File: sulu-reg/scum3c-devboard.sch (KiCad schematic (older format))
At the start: 36 parts, among them J1 Conn_02x11_Odd_Even, J2 Conn_02x10_Odd_Even, J3 Conn_02x05_Odd_Even, J4 Conn_01x01_Male, U2 S-85S1AB18-I6T1U, U3 S-85S1AB11-I6T1U, U9AB1 ICM-20948

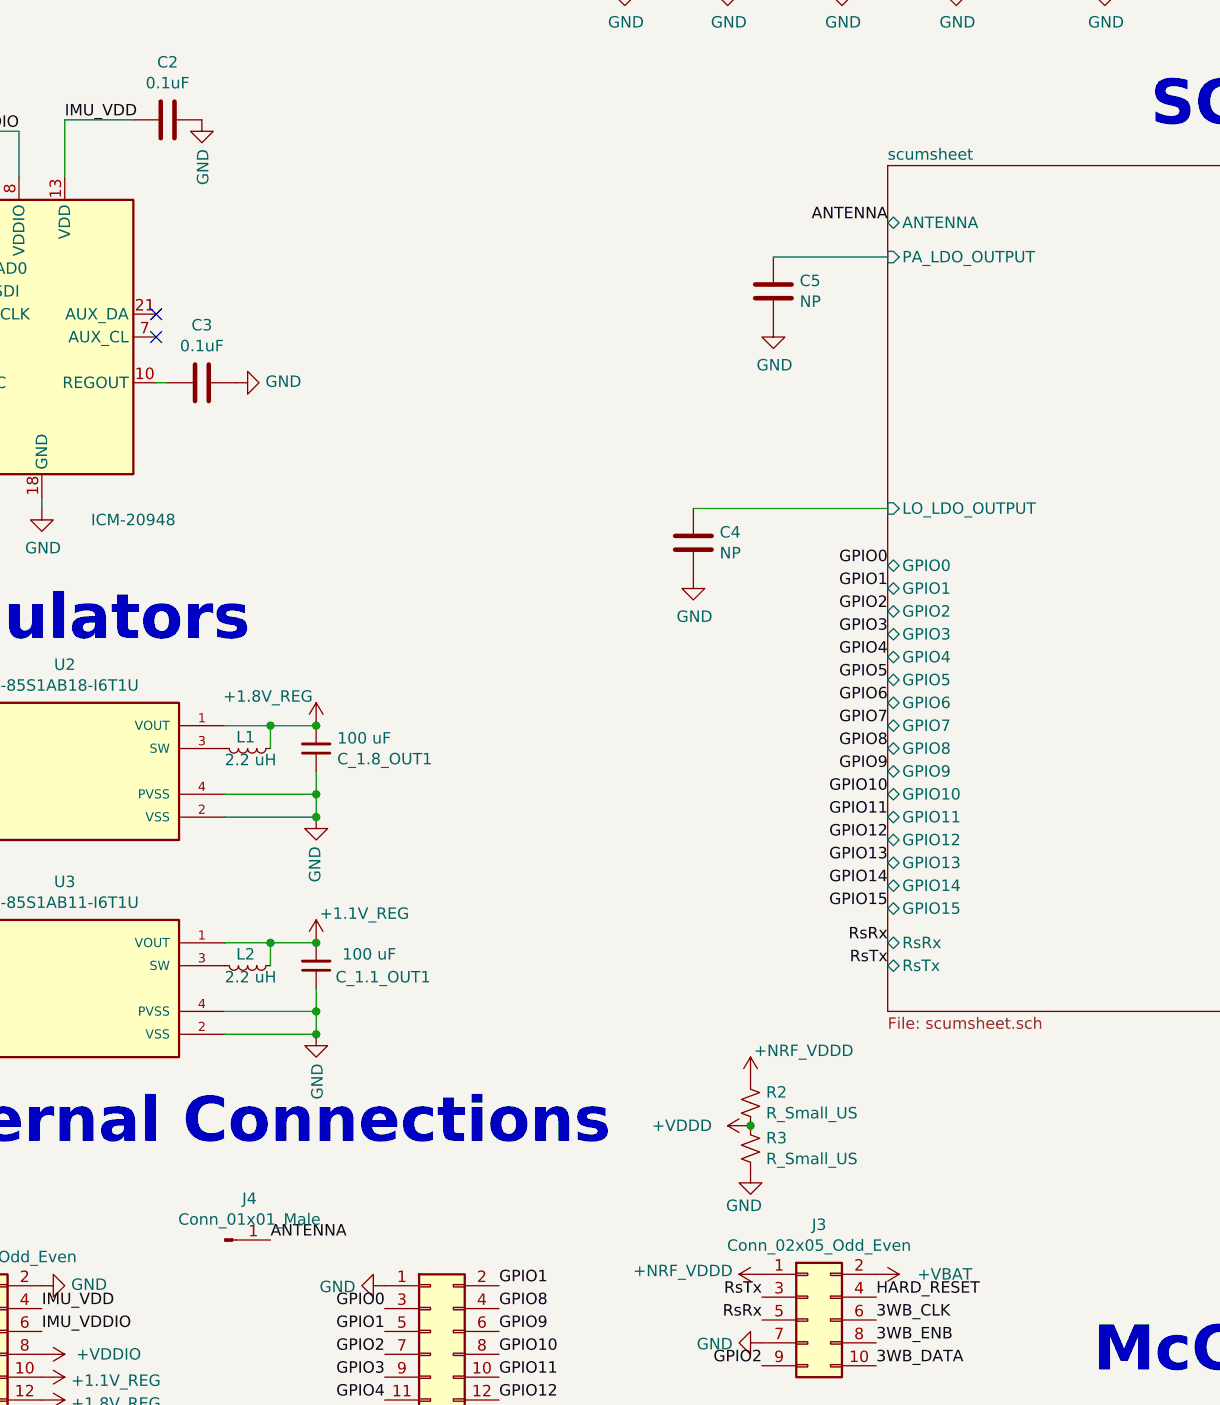
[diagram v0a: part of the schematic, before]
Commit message: added coax connector, not connected in layout
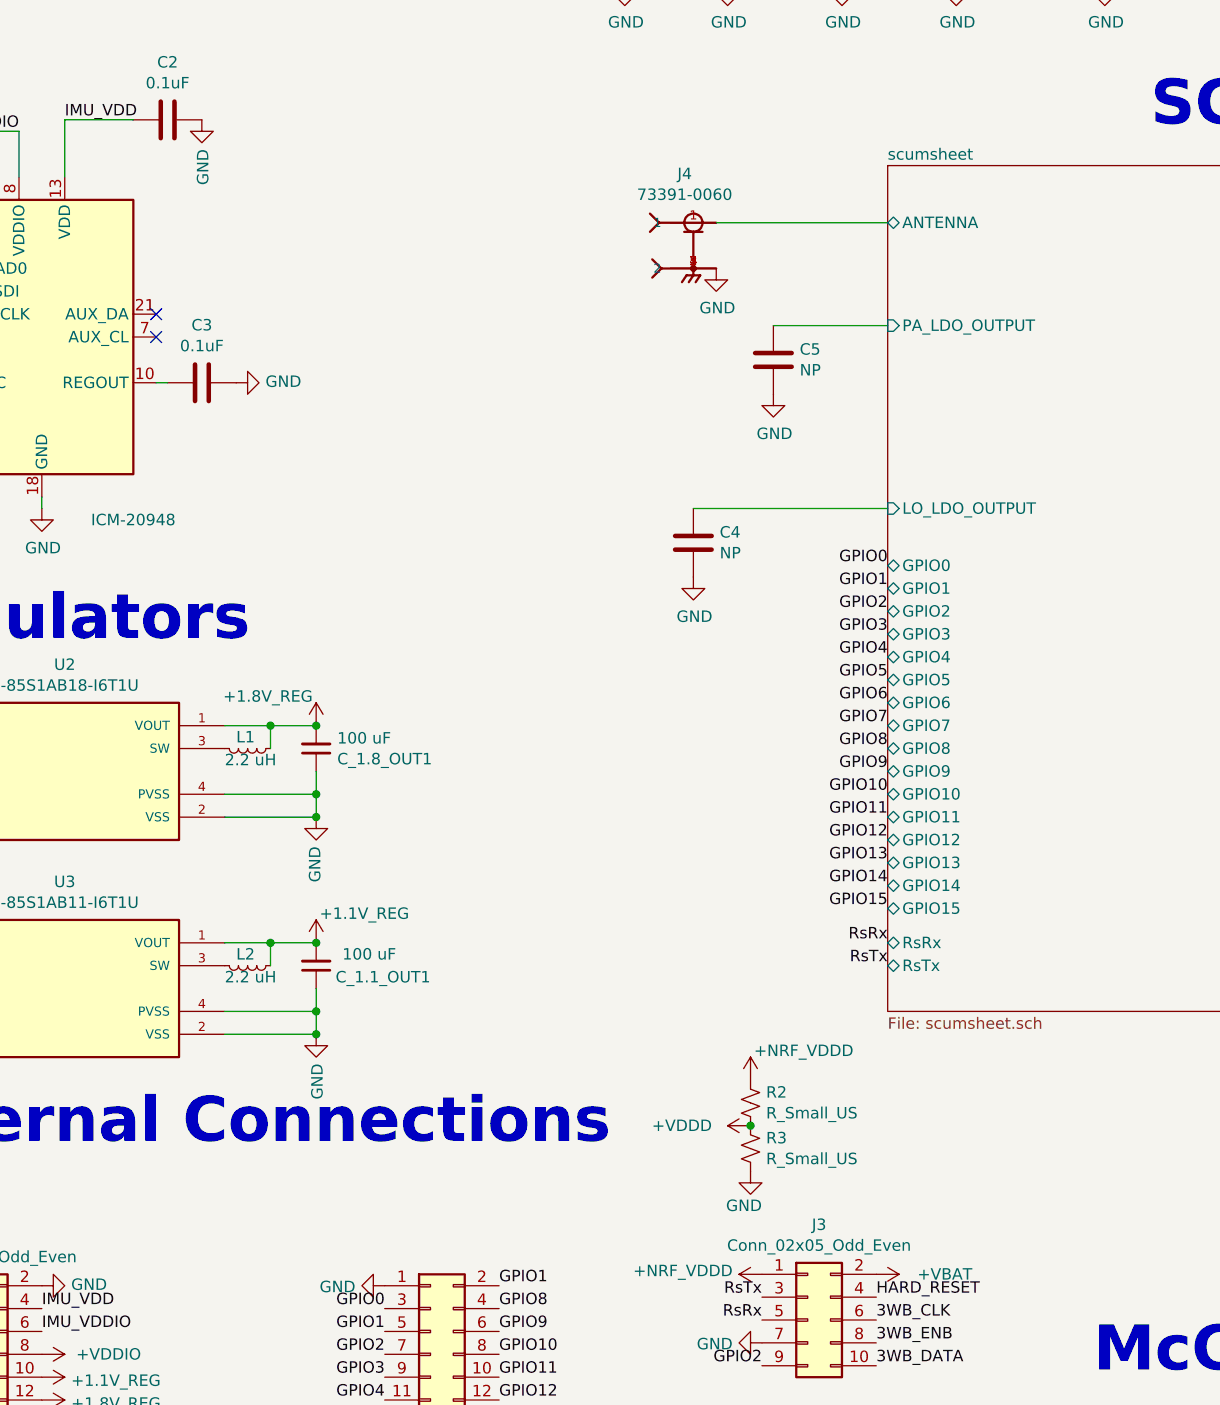
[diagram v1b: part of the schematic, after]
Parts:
- removed J4: Conn_01x01_Male, Connector_PinHeader_2.54mm:PinHeader_1x01_P2.54mm_Vertical, symbol Connector:Conn_01x01_Male
- added J4: 73391-0060, downloaded_libs:MOLEX_73391-0060, symbol 73391-0060:73391-0060
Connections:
- net GND: now also J4.2, J4.3 (2), J4.4 (2), J4.5 (2)
- new net scumsheet/ANTENNA: J4.1
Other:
- moved on the sheet: C5
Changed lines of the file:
@@
 Text Notes 6400 7200 0    197  ~ 39
 McCoy PCB v1.1
-Text Label 2800 6600 0    50   ~ 0
-ANTENNA
-Text Label 5500 2150 2    50   ~ 0
-ANTENNA
 Text Label 7950 3600 0    50   ~ 0
 HARD_RESET
@@
 F27 "GPIO11" B L 5500 4750 50
 F28 "LO_LDO_OUTPUT" I L 5500 3400 50
-F29 "PA_LDO_OUTPUT" I L 5500 2300 50
+F29 "PA_LDO_OUTPUT" I L 5500 2600 50
 F30 "AUX_LDO_OUTPUT" I R 7950 2850 50
 F31 "VDDD_LDO_OUTPUT" I R 7950 2650 50
@@
 L Device:C C?
 U 1 1 60877945
-P 5000 2450
+P 5000 2750
 AR Path="/5F3B1D81/60877945" Ref="C?"  Part="1"
 AR Path="/5F41418C/60877945" Ref="C?"  Part="1"
 AR Path="/5F414989/60877945" Ref="C?"  Part="1"
 AR Path="/60877945" Ref="C5"  Part="1"
-F 0 "C5" H 5115 2496 50  0000 L CNN
-F 1 "NP" H 5115 2405 50  0000 L CNN
-F 2 "Capacitor_SMD:C_0402_1005Metric" H 5038 2300 50  0001 C CNN
-F 3 "~" H 5000 2450 50  0001 C CNN
-	1    5000 2450
+F 0 "C5" H 5115 2796 50  0000 L CNN
+F 1 "NP" H 5115 2705 50  0000 L CNN
+F 2 "Capacitor_SMD:C_0402_1005Metric" H 5038 2600 50  0001 C CNN
+F 3 "~" H 5000 2750 50  0001 C CNN
+	1    5000 2750
 	1    0    0    -1
 $EndComp
@@
 L power:GND #PWR?
 U 1 1 6087794B
-P 5000 2600
+P 5000 2900
 AR Path="/5F3B1D81/6087794B" Ref="#PWR?"  Part="1"
 AR Path="/5F41418C/6087794B" Ref="#PWR?"  Part="1"
 AR Path="/5F414989/6087794B" Ref="#PWR?"  Part="1"
 AR Path="/6087794B" Ref="#PWR014"  Part="1"
-F 0 "#PWR014" H 5000 2350 50  0001 C CNN
-F 1 "GND" H 5005 2427 50  0000 C CNN
-F 2 "" H 5000 2600 50  0001 C CNN
-F 3 "" H 5000 2600 50  0001 C CNN
-	1    5000 2600
+F 0 "#PWR014" H 5000 2650 50  0001 C CNN
+F 1 "GND" H 5005 2727 50  0000 C CNN
+F 2 "" H 5000 2900 50  0001 C CNN
+F 3 "" H 5000 2900 50  0001 C CNN
+	1    5000 2900
 	1    0    0    -1
 $EndComp
@@
 $EndComp
 Wire Wire Line
-	5500 2300 5000 2300
+	5500 2600 5000 2600
 Wire Wire Line
 	5500 3400 4650 3400
@@
 GPIO2
 $Comp
-L Connector:Conn_01x01_Male J4
-U 1 1 6088AE2D
-P 2600 6600
-F 0 "J4" H 2708 6781 50  0000 C CNN
-F 1 "Conn_01x01_Male" H 2708 6690 50  0000 C CNN
-F 2 "Connector_PinHeader_2.54mm:PinHeader_1x01_P2.54mm_Vertical" H 2600 6600 50  0001 C CNN
-F 3 "~" H 2600 6600 50  0001 C CNN
-	1    2600 6600
-	1    0    0    -1
-$EndComp
-$Comp
 L draft1library:+VBAT #PWR?
 U 1 1 6127ADAC
@@
 	0    1    1    0
 $EndComp
+$Comp
+L power:GND #PWR?
+U 1 1 613258AF
+P 4750 2350
+AR Path="/5F3B1D81/613258AF" Ref="#PWR?"  Part="1"
+AR Path="/5F41418C/613258AF" Ref="#PWR?"  Part="1"
+AR Path="/5F414989/613258AF" Ref="#PWR?"  Part="1"
+AR Path="/613258AF" Ref="#PWR0129"  Part="1"
+F 0 "#PWR0129" H 4750 2100 50  0001 C CNN
+F 1 "GND" H 4755 2177 50  0000 C CNN
+F 2 "" H 4750 2350 50  0001 C CNN
+F 3 "" H 4750 2350 50  0001 C CNN
+	1    4750 2350
+	1    0    0    -1
+$EndComp
+Wire Wire Line
+	5500 2150 4750 2150
+$Comp
+L 73391-0060:73391-0060 J4
+U 1 1 613314E8
+P 4650 2250
+F 0 "J4" H 4612 2564 50  0000 C CNN
+F 1 "73391-0060" H 4612 2473 50  0000 C CNN
+F 2 "downloaded_libs:MOLEX_73391-0060" H 4650 2250 50  0001 L BNN
+F 3 "" H 4650 2250 50  0001 L BNN
+F 4 "Molex" H 4650 2250 50  0001 L BNN "MANUFACTURER"
+	1    4650 2250
+	1    0    0    -1
+$EndComp
 $EndSCHEMATC

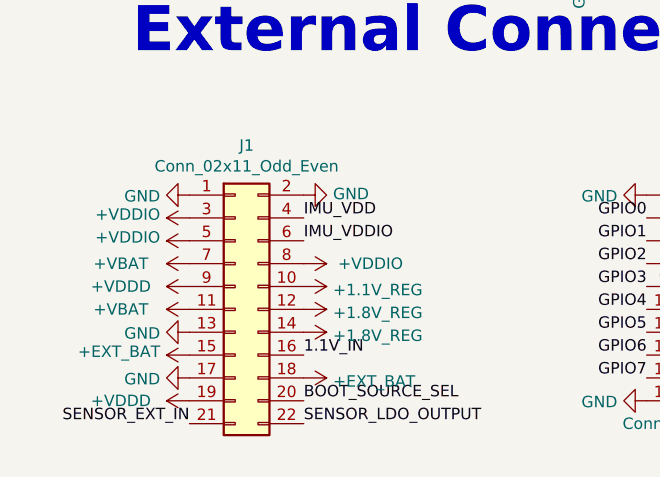
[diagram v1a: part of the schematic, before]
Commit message: connected most things on the north headers
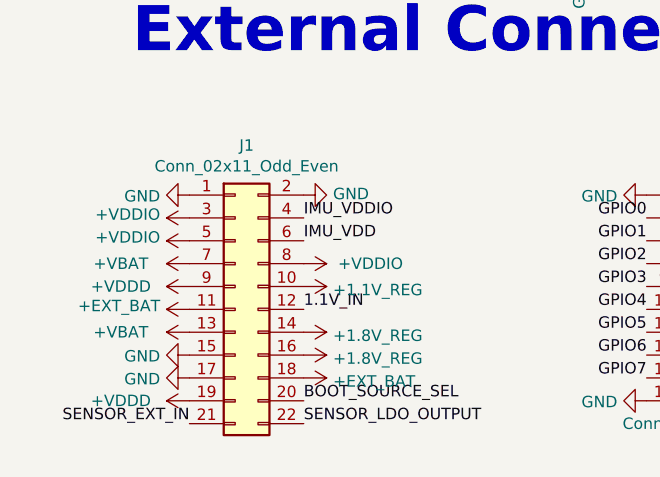
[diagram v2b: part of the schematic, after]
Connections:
- net +1.8V_REG: now also J1.16 (Pin_16); no longer J1.12 (Pin_12)
- net +EXT_BAT: now also J1.11 (Pin_11); no longer J1.15 (Pin_15)
- net +VBAT: now also J1.13 (Pin_13); no longer J1.11 (Pin_11)
- net 1.1V_IN: now also J1.12 (Pin_12); no longer J1.16 (Pin_16)
- net GND: now also J1.15 (Pin_15); no longer J1.13 (Pin_13)
- net IMU_VDD: now also J1.6 (Pin_6); no longer J1.4 (Pin_4)
- net IMU_VDDIO: now also J1.4 (Pin_4); no longer J1.6 (Pin_6)
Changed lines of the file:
@@
 Text Label 1700 1750 2    50   ~ 0
 IMU_VDDIO
-Text Label 1800 7000 0    50   ~ 0
+Text Label 1800 6900 0    50   ~ 0
 IMU_VDDIO
 Text Label 3800 7300 0    50   ~ 0
@@
 Text Label 3800 7600 0    50   ~ 0
 GPIO15
-Text Label 1800 6900 0    50   ~ 0
+Text Label 1800 7000 0    50   ~ 0
 IMU_VDD
 NoConn ~ 1300 2950
@@
 L draft1library:+VBAT #PWR?
 U 1 1 6127ADAC
-P 1300 7300
+P 1300 7400
 AR Path="/5F3B1D81/6127ADAC" Ref="#PWR?"  Part="1"
 AR Path="/5F41418C/6127ADAC" Ref="#PWR?"  Part="1"
 AR Path="/5F414989/6127ADAC" Ref="#PWR?"  Part="1"
 AR Path="/6127ADAC" Ref="#PWR0107"  Part="1"
-F 0 "#PWR0107" H 1300 7150 50  0001 C CNN
-F 1 "+VBAT" V 1300 7600 50  0000 C CNN
-F 2 "" H 1300 7300 50  0001 C CNN
-F 3 "" H 1300 7300 50  0001 C CNN
-	1    1300 7300
-	0    -1   -1   0
-$EndComp
-$Comp
-L power:GND #PWR0108
-U 1 1 6127B18B
-P 1300 7400
-F 0 "#PWR0108" H 1300 7150 50  0001 C CNN
-F 1 "GND" V 1305 7272 50  0000 R CNN
+F 0 "#PWR0107" H 1300 7250 50  0001 C CNN
+F 1 "+VBAT" V 1300 7700 50  0000 C CNN
 F 2 "" H 1300 7400 50  0001 C CNN
 F 3 "" H 1300 7400 50  0001 C CNN
 	1    1300 7400
+	0    -1   -1   0
+$EndComp
+$Comp
+L power:GND #PWR0108
+U 1 1 6127B18B
+P 1300 7500
+F 0 "#PWR0108" H 1300 7250 50  0001 C CNN
+F 1 "GND" V 1305 7372 50  0000 R CNN
+F 2 "" H 1300 7500 50  0001 C CNN
+F 3 "" H 1300 7500 50  0001 C CNN
+	1    1300 7500
 	0    1    1    0
 $EndComp
@@
 L draft1library:+1.8V_REG #PWR0111
 U 1 1 61281B91
-P 1800 7300
-F 0 "#PWR0111" H 1800 7150 50  0001 C CNN
-F 1 "+1.8V_REG" V 1815 7428 50  0000 L CNN
-F 2 "" H 1800 7300 50  0001 C CNN
-F 3 "" H 1800 7300 50  0001 C CNN
-	1    1800 7300
-	0    1    1    0
-$EndComp
-$Comp
-L draft1library:+1.8V_REG #PWR0112
-U 1 1 612829BE
 P 1800 7400
-F 0 "#PWR0112" H 1800 7250 50  0001 C CNN
+F 0 "#PWR0111" H 1800 7250 50  0001 C CNN
 F 1 "+1.8V_REG" V 1815 7528 50  0000 L CNN
 F 2 "" H 1800 7400 50  0001 C CNN
 F 3 "" H 1800 7400 50  0001 C CNN
 	1    1800 7400
+	0    1    1    0
+$EndComp
+$Comp
+L draft1library:+1.8V_REG #PWR0112
+U 1 1 612829BE
+P 1800 7500
+F 0 "#PWR0112" H 1800 7350 50  0001 C CNN
+F 1 "+1.8V_REG" V 1815 7628 50  0000 L CNN
+F 2 "" H 1800 7500 50  0001 C CNN
+F 3 "" H 1800 7500 50  0001 C CNN
+	1    1800 7500
 	0    1    1    0
 $EndComp
@@
 	1    0    0    -1
 $EndComp
-Text Label 1800 7500 0    50   ~ 0
+Text Label 1800 7300 0    50   ~ 0
 1.1V_IN
 $Comp
 L draft1library:+EXT_BAT #PWR0123
 U 1 1 6136676E
-P 1300 7500
-F 0 "#PWR0123" H 1300 7350 50  0001 C CNN
-F 1 "+EXT_BAT" V 1315 7628 50  0000 L CNN
-F 2 "" H 1300 7500 50  0001 C CNN
-F 3 "" H 1300 7500 50  0001 C CNN
-	1    1300 7500
-	0    -1   -1   0
-$EndComp
+P 1300 7300
+F 0 "#PWR0123" H 1300 7150 50  0001 C CNN
+F 1 "+EXT_BAT" V 1315 7428 50  0000 L CNN
+F 2 "" H 1300 7300 50  0001 C CNN
+F 3 "" H 1300 7300 50  0001 C CNN
+	1    1300 7300
+	0    -1   -1   0
+$EndComp
